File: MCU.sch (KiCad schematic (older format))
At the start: 66 parts, among them SW1 SW_Push, U1 STM32F407IGTx, Y1 12MHz, 20pF

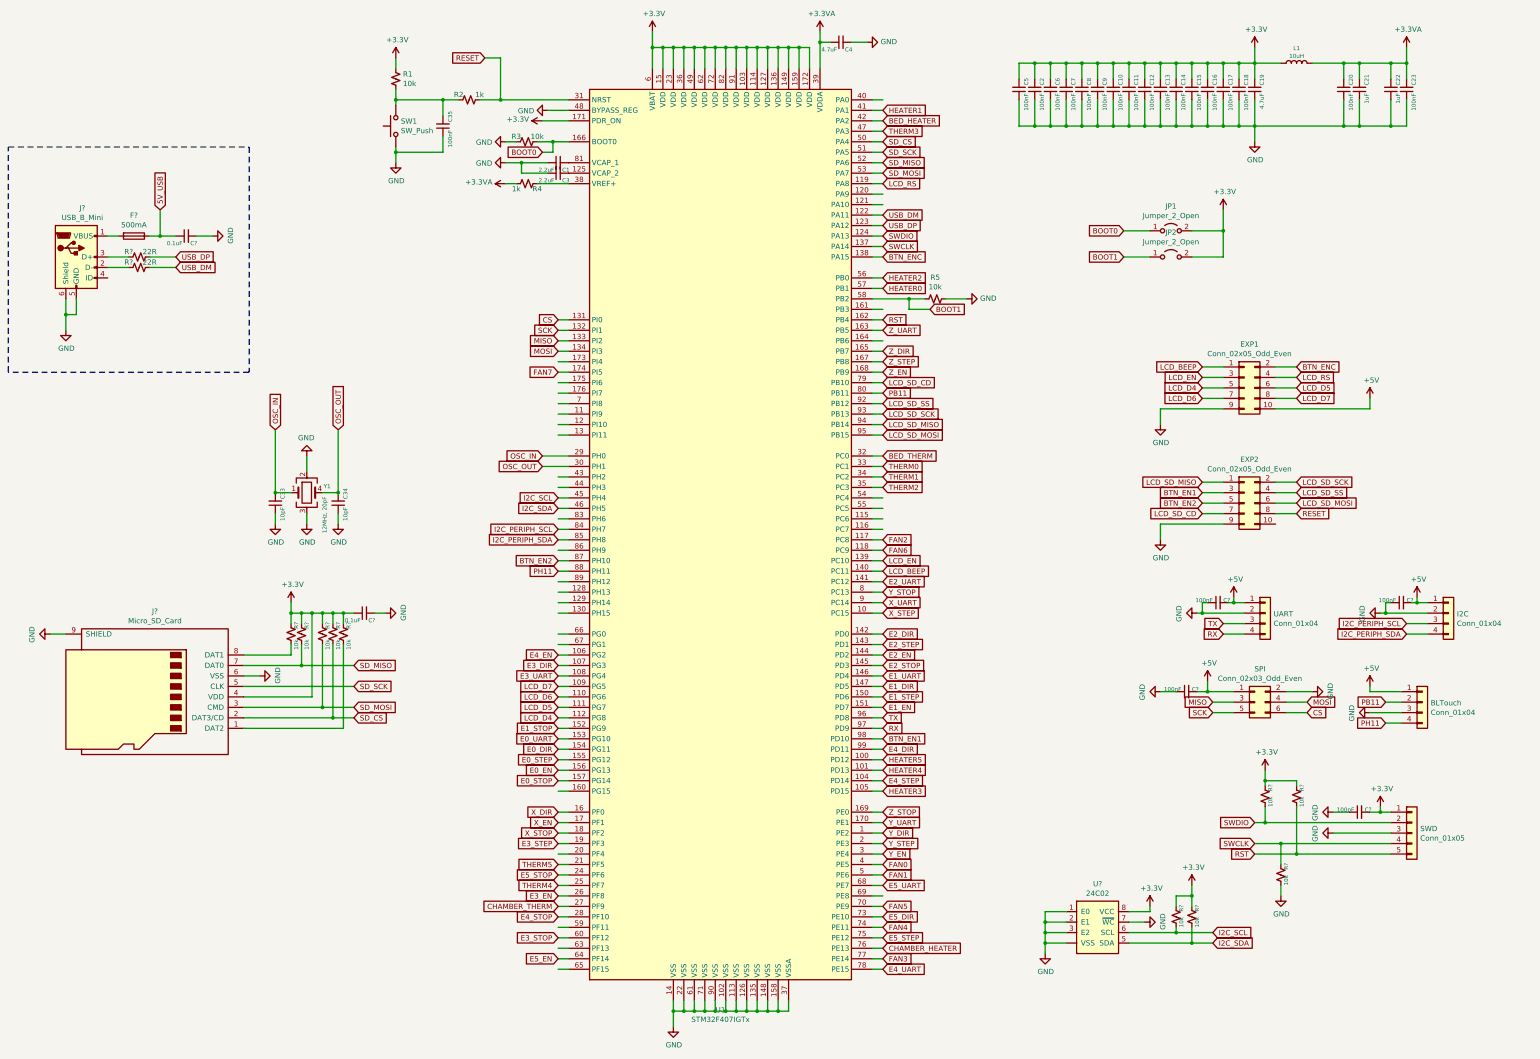
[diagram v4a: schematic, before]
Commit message: added raspberry pi header
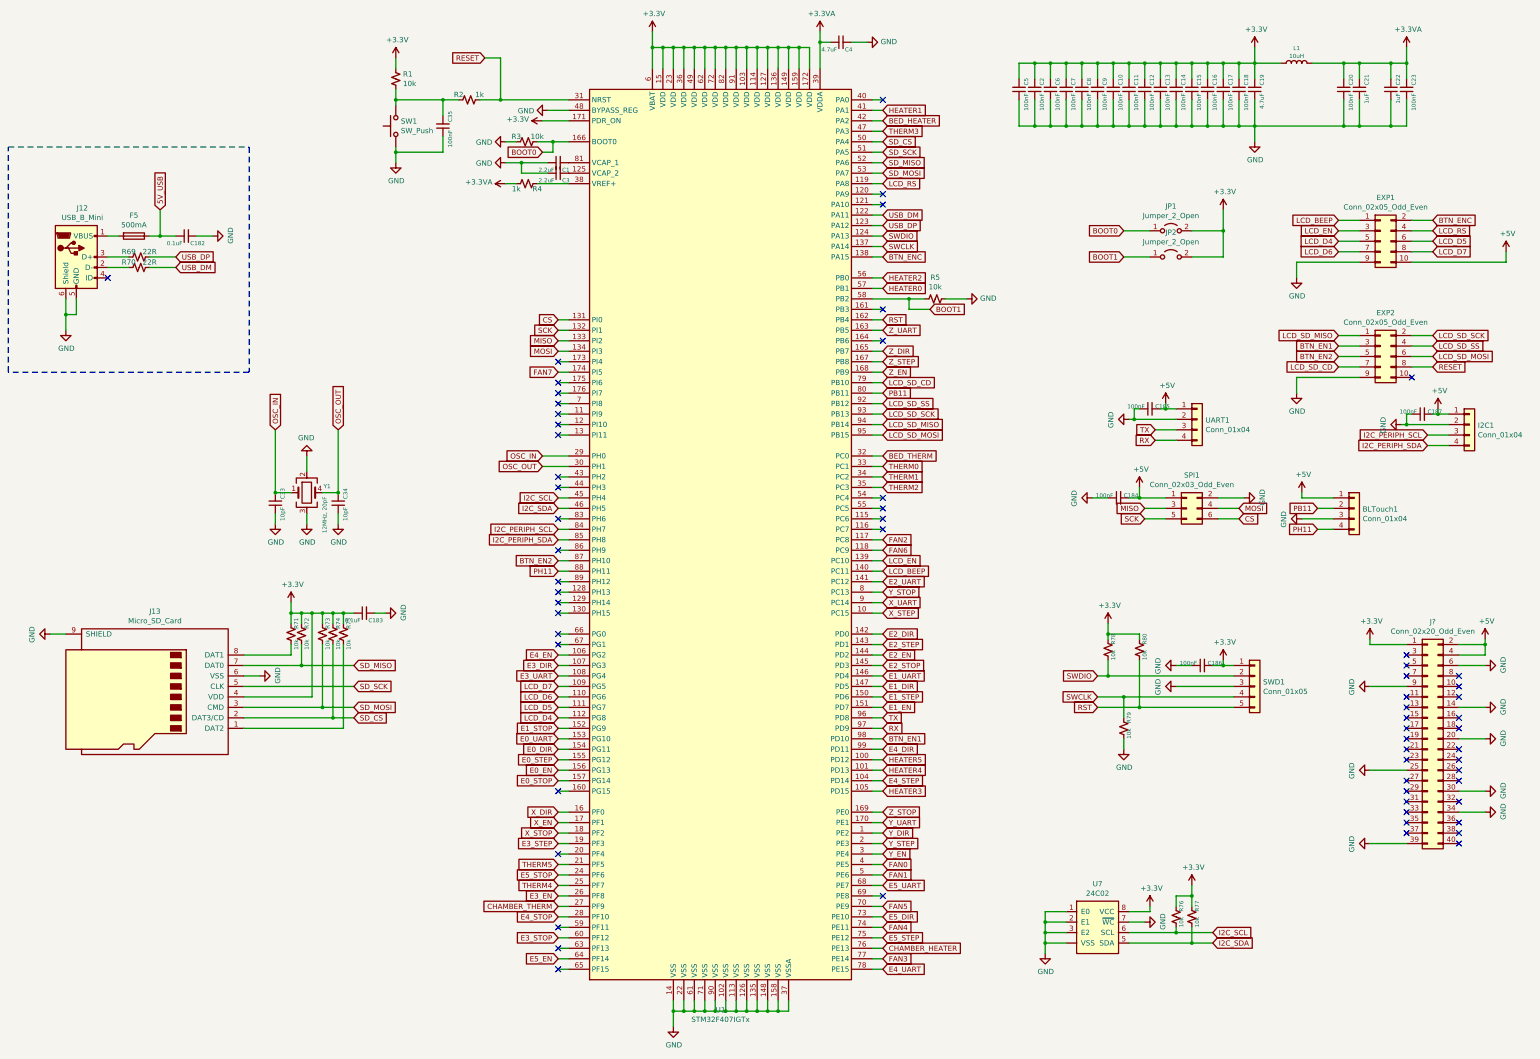
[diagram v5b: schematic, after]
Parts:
- added J?: Conn_02x20_Odd_Even, symbol Connector_Generic:Conn_02x20_Odd_Even
- gave numbers to parts that had none: 22
- renumbered BLTouch to BLTouch1, I2C to I2C1, SPI to SPI1, SWD to SWD1, UART to UART1
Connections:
- wire segments 465 -> 479
- no-connect marks 0 -> 63
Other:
- moved on the sheet: BLTouch1, C184, C185, C186, C187, EXP1, EXP2, I2C1, R78, R79, R80, SPI1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

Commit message: added library
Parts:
- gave numbers to parts that had none: 1
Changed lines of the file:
@@
 NoConn ~ 6350 5650
 $Comp
-L Connector_Generic:Conn_02x20_Odd_Even J?
+L Connector_Generic:Conn_02x20_Odd_Even J55
 U 1 1 61D58D2C
 P 14650 7450
-F 0 "J?" H 14700 8567 50  0000 C CNN
+F 0 "J55" H 14700 8567 50  0000 C CNN
 F 1 "Conn_02x20_Odd_Even" H 14700 8476 50  0000 C CNN
 F 2 "" H 14650 7450 50  0001 C CNN
@@
 $EndComp
 $Comp
-L power:+5V #PWR?
+L power:+5V #PWR0278
 U 1 1 61D5B6B4
 P 15200 6500
-F 0 "#PWR?" H 15200 6350 50  0001 C CNN
+F 0 "#PWR0278" H 15200 6350 50  0001 C CNN
 F 1 "+5V" H 15215 6673 50  0000 C CNN
 F 2 "" H 15200 6500 50  0001 C CNN
@@
 $EndComp
 $Comp
-L power:GND #PWR?
+L power:GND #PWR0279
 U 1 1 61D5BD7A
 P 15200 7950
-F 0 "#PWR?" H 15200 7700 50  0001 C CNN
+F 0 "#PWR0279" H 15200 7700 50  0001 C CNN
 F 1 "GND" H 15205 7777 50  0000 C CNN
 F 2 "" H 15200 7950 50  0001 C CNN
@@
 $EndComp
 $Comp
-L power:+3.3V #PWR?
+L power:+3.3V #PWR0280
 U 1 1 61D5BEF0
 P 14100 6500
-F 0 "#PWR?" H 14100 6350 50  0001 C CNN
+F 0 "#PWR0280" H 14100 6350 50  0001 C CNN
 F 1 "+3.3V" H 14115 6673 50  0000 C CNN
 F 2 "" H 14100 6500 50  0001 C CNN
@@
 Connection ~ 15200 6550
 $Comp
-L power:GND #PWR?
+L power:GND #PWR0281
 U 1 1 61E37426
 P 15200 6750
-F 0 "#PWR?" H 15200 6500 50  0001 C CNN
+F 0 "#PWR0281" H 15200 6500 50  0001 C CNN
 F 1 "GND" H 15205 6577 50  0000 C CNN
 F 2 "" H 15200 6750 50  0001 C CNN
@@
 $EndComp
 $Comp
-L power:GND #PWR?
+L power:GND #PWR0282
 U 1 1 61E375CC
 P 14100 6950
-F 0 "#PWR?" H 14100 6700 50  0001 C CNN
+F 0 "#PWR0282" H 14100 6700 50  0001 C CNN
 F 1 "GND" H 14105 6777 50  0000 C CNN
 F 2 "" H 14100 6950 50  0001 C CNN
@@
 $EndComp
 $Comp
-L power:GND #PWR?
+L power:GND #PWR0283
 U 1 1 61E378A8
 P 15200 7450
-F 0 "#PWR?" H 15200 7200 50  0001 C CNN
+F 0 "#PWR0283" H 15200 7200 50  0001 C CNN
 F 1 "GND" H 15205 7277 50  0000 C CNN
 F 2 "" H 15200 7450 50  0001 C CNN
@@
 $EndComp
 $Comp
-L power:GND #PWR?
+L power:GND #PWR0284
 U 1 1 61E37F4E
 P 15200 8150
-F 0 "#PWR?" H 15200 7900 50  0001 C CNN
+F 0 "#PWR0284" H 15200 7900 50  0001 C CNN
 F 1 "GND" H 15205 7977 50  0000 C CNN
 F 2 "" H 15200 8150 50  0001 C CNN
@@
 $EndComp
 $Comp
-L power:GND #PWR?
+L power:GND #PWR0285
 U 1 1 61E38209
 P 14100 7750
-F 0 "#PWR?" H 14100 7500 50  0001 C CNN
+F 0 "#PWR0285" H 14100 7500 50  0001 C CNN
 F 1 "GND" H 14105 7577 50  0000 C CNN
 F 2 "" H 14100 7750 50  0001 C CNN
@@
 $EndComp
 $Comp
-L power:GND #PWR?
+L power:GND #PWR0286
 U 1 1 61E38767
 P 14100 8450
-F 0 "#PWR?" H 14100 8200 50  0001 C CNN
+F 0 "#PWR0286" H 14100 8200 50  0001 C CNN
 F 1 "GND" H 14105 8277 50  0000 C CNN
 F 2 "" H 14100 8450 50  0001 C CNN
@@
 	15200 8150 14950 8150
 $Comp
-L power:GND #PWR?
+L power:GND #PWR0287
 U 1 1 62041588
 P 15200 7150
-F 0 "#PWR?" H 15200 6900 50  0001 C CNN
+F 0 "#PWR0287" H 15200 6900 50  0001 C CNN
 F 1 "GND" H 15205 6977 50  0000 C CNN
 F 2 "" H 15200 7150 50  0001 C CNN

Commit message: assigned some footprints
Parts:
- C10, C11, C12, C13, C14, C15, C16, C17, C18, C182, C183, C184, C185, C186, C187, C2, C20, C21, C22, C23, C35, C5, C6, C7, C8, C9: footprint (none) -> Capacitor_SMD:C_0603_1608Metric_Pad1.05x0.95mm_HandSolder
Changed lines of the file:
@@
 F 0 "C2" V 10808 1212 39  0000 R TNN
 F 1 "100nF" V 10808 1287 39  0000 L TNN
-F 2 "" H 10900 1250 50  0001 C CNN
+F 2 "Capacitor_SMD:C_0603_1608Metric_Pad1.05x0.95mm_HandSolder" H 10900 1250 50  0001 C CNN
 F 3 "~" H 10900 1250 50  0001 C CNN
 	1    10900 1250
@@
 F 0 "C6" V 10958 1212 39  0000 R TNN
 F 1 "100nF" V 10958 1287 39  0000 L TNN
-F 2 "" H 11050 1250 50  0001 C CNN
+F 2 "Capacitor_SMD:C_0603_1608Metric_Pad1.05x0.95mm_HandSolder" H 11050 1250 50  0001 C CNN
 F 3 "~" H 11050 1250 50  0001 C CNN
 	1    11050 1250
@@
 F 0 "C7" V 11108 1212 39  0000 R TNN
 F 1 "100nF" V 11108 1287 39  0000 L TNN
-F 2 "" H 11200 1250 50  0001 C CNN
+F 2 "Capacitor_SMD:C_0603_1608Metric_Pad1.05x0.95mm_HandSolder" H 11200 1250 50  0001 C CNN
 F 3 "~" H 11200 1250 50  0001 C CNN
 	1    11200 1250
@@
 F 0 "C8" V 11258 1212 39  0000 R TNN
 F 1 "100nF" V 11258 1287 39  0000 L TNN
-F 2 "" H 11350 1250 50  0001 C CNN
+F 2 "Capacitor_SMD:C_0603_1608Metric_Pad1.05x0.95mm_HandSolder" H 11350 1250 50  0001 C CNN
 F 3 "~" H 11350 1250 50  0001 C CNN
 	1    11350 1250
@@
 F 0 "C9" V 11408 1212 39  0000 R TNN
 F 1 "100nF" V 11408 1287 39  0000 L TNN
-F 2 "" H 11500 1250 50  0001 C CNN
+F 2 "Capacitor_SMD:C_0603_1608Metric_Pad1.05x0.95mm_HandSolder" H 11500 1250 50  0001 C CNN
 F 3 "~" H 11500 1250 50  0001 C CNN
 	1    11500 1250
@@
 F 0 "C10" V 11558 1212 39  0000 R TNN
 F 1 "100nF" V 11558 1287 39  0000 L TNN
-F 2 "" H 11650 1250 50  0001 C CNN
+F 2 "Capacitor_SMD:C_0603_1608Metric_Pad1.05x0.95mm_HandSolder" H 11650 1250 50  0001 C CNN
 F 3 "~" H 11650 1250 50  0001 C CNN
 	1    11650 1250
@@
 F 0 "C11" V 11708 1212 39  0000 R TNN
 F 1 "100nF" V 11708 1287 39  0000 L TNN
-F 2 "" H 11800 1250 50  0001 C CNN
+F 2 "Capacitor_SMD:C_0603_1608Metric_Pad1.05x0.95mm_HandSolder" H 11800 1250 50  0001 C CNN
 F 3 "~" H 11800 1250 50  0001 C CNN
 	1    11800 1250
@@
 F 0 "C12" V 11858 1212 39  0000 R TNN
 F 1 "100nF" V 11858 1287 39  0000 L TNN
-F 2 "" H 11950 1250 50  0001 C CNN
+F 2 "Capacitor_SMD:C_0603_1608Metric_Pad1.05x0.95mm_HandSolder" H 11950 1250 50  0001 C CNN
 F 3 "~" H 11950 1250 50  0001 C CNN
 	1    11950 1250
@@
 F 0 "C13" V 12008 1212 39  0000 R TNN
 F 1 "100nF" V 12008 1287 39  0000 L TNN
-F 2 "" H 12100 1250 50  0001 C CNN
+F 2 "Capacitor_SMD:C_0603_1608Metric_Pad1.05x0.95mm_HandSolder" H 12100 1250 50  0001 C CNN
 F 3 "~" H 12100 1250 50  0001 C CNN
 	1    12100 1250
@@
 F 0 "C14" V 12158 1212 39  0000 R TNN
 F 1 "100nF" V 12158 1287 39  0000 L TNN
-F 2 "" H 12250 1250 50  0001 C CNN
+F 2 "Capacitor_SMD:C_0603_1608Metric_Pad1.05x0.95mm_HandSolder" H 12250 1250 50  0001 C CNN
 F 3 "~" H 12250 1250 50  0001 C CNN
 	1    12250 1250
@@
 F 0 "C5" V 10658 1212 39  0000 R TNN
 F 1 "100nF" V 10658 1287 39  0000 L TNN
-F 2 "" H 10750 1250 50  0001 C CNN
+F 2 "Capacitor_SMD:C_0603_1608Metric_Pad1.05x0.95mm_HandSolder" H 10750 1250 50  0001 C CNN
 F 3 "~" H 10750 1250 50  0001 C CNN
 	1    10750 1250
@@
 F 0 "C15" V 12308 1212 39  0000 R TNN
 F 1 "100nF" V 12308 1287 39  0000 L TNN
-F 2 "" H 12400 1250 50  0001 C CNN
+F 2 "Capacitor_SMD:C_0603_1608Metric_Pad1.05x0.95mm_HandSolder" H 12400 1250 50  0001 C CNN
 F 3 "~" H 12400 1250 50  0001 C CNN
 	1    12400 1250
@@
 F 0 "C16" V 12458 1212 39  0000 R TNN
 F 1 "100nF" V 12458 1287 39  0000 L TNN
-F 2 "" H 12550 1250 50  0001 C CNN
+F 2 "Capacitor_SMD:C_0603_1608Metric_Pad1.05x0.95mm_HandSolder" H 12550 1250 50  0001 C CNN
 F 3 "~" H 12550 1250 50  0001 C CNN
 	1    12550 1250
@@
 F 0 "C17" V 12608 1212 39  0000 R TNN
 F 1 "100nF" V 12608 1287 39  0000 L TNN
-F 2 "" H 12700 1250 50  0001 C CNN
+F 2 "Capacitor_SMD:C_0603_1608Metric_Pad1.05x0.95mm_HandSolder" H 12700 1250 50  0001 C CNN
 F 3 "~" H 12700 1250 50  0001 C CNN
 	1    12700 1250
@@
 F 0 "C18" V 12758 1212 39  0000 R TNN
 F 1 "100nF" V 12758 1287 39  0000 L TNN
-F 2 "" H 12850 1250 50  0001 C CNN
+F 2 "Capacitor_SMD:C_0603_1608Metric_Pad1.05x0.95mm_HandSolder" H 12850 1250 50  0001 C CNN
 F 3 "~" H 12850 1250 50  0001 C CNN
 	1    12850 1250
@@
 F 0 "C20" V 13758 1212 39  0000 R TNN
 F 1 "100nF" V 13758 1287 39  0000 L TNN
-F 2 "" H 13850 1250 50  0001 C CNN
+F 2 "Capacitor_SMD:C_0603_1608Metric_Pad1.05x0.95mm_HandSolder" H 13850 1250 50  0001 C CNN
 F 3 "~" H 13850 1250 50  0001 C CNN
 	1    13850 1250
@@
 F 0 "C21" V 13908 1212 39  0000 R TNN
 F 1 "1uF" V 13908 1287 39  0000 L TNN
-F 2 "" H 14000 1250 50  0001 C CNN
+F 2 "Capacitor_SMD:C_0603_1608Metric_Pad1.05x0.95mm_HandSolder" H 14000 1250 50  0001 C CNN
 F 3 "~" H 14000 1250 50  0001 C CNN
 	1    14000 1250
@@
 F 0 "C22" V 14208 1212 39  0000 R TNN
 F 1 "1uF" V 14208 1287 39  0000 L TNN
-F 2 "" H 14300 1250 50  0001 C CNN
+F 2 "Capacitor_SMD:C_0603_1608Metric_Pad1.05x0.95mm_HandSolder" H 14300 1250 50  0001 C CNN
 F 3 "~" H 14300 1250 50  0001 C CNN
 	1    14300 1250
@@
 F 0 "C23" V 14358 1212 39  0000 R TNN
 F 1 "100nF" V 14358 1287 39  0000 L TNN
-F 2 "" H 14450 1250 50  0001 C CNN
+F 2 "Capacitor_SMD:C_0603_1608Metric_Pad1.05x0.95mm_HandSolder" H 14450 1250 50  0001 C CNN
 F 3 "~" H 14450 1250 50  0001 C CNN
 	1    14450 1250
@@
 F 0 "C35" V 5158 1562 39  0000 R TNN
 F 1 "100nF" V 5158 1637 39  0000 L TNN
-F 2 "" H 5250 1600 50  0001 C CNN
+F 2 "Capacitor_SMD:C_0603_1608Metric_Pad1.05x0.95mm_HandSolder" H 5250 1600 50  0001 C CNN
 F 3 "~" H 5250 1600 50  0001 C CNN
 	1    5250 1600
@@
 F 0 "C182" V 2708 2612 39  0000 R TNN
 F 1 "0.1uF" V 2708 2687 39  0000 L TNN
-F 2 "" H 2800 2650 50  0001 C CNN
+F 2 "Capacitor_SMD:C_0603_1608Metric_Pad1.05x0.95mm_HandSolder" H 2800 2650 50  0001 C CNN
 F 3 "~" H 2800 2650 50  0001 C CNN
 	1    2800 2650
@@
 F 0 "C183" V 4408 6212 39  0000 R TNN
 F 1 "0.1uF" V 4408 6287 39  0000 L TNN
-F 2 "" H 4500 6250 50  0001 C CNN
+F 2 "Capacitor_SMD:C_0603_1608Metric_Pad1.05x0.95mm_HandSolder" H 4500 6250 50  0001 C CNN
 F 3 "~" H 4500 6250 50  0001 C CNN
 	1    4500 6250
@@
 F 0 "C187" V 14600 4300 39  0000 R TNN
 F 1 "100nF" V 14600 4400 39  0000 L TNN
-F 2 "" H 14600 4350 50  0001 C CNN
+F 2 "Capacitor_SMD:C_0603_1608Metric_Pad1.05x0.95mm_HandSolder" H 14600 4350 50  0001 C CNN
 F 3 "~" H 14600 4350 50  0001 C CNN
 	1    14600 4350
@@
 F 0 "C184" V 11700 5100 39  0000 R TNN
 F 1 "100nF" V 11700 5200 39  0000 L TNN
-F 2 "" H 11700 5150 50  0001 C CNN
+F 2 "Capacitor_SMD:C_0603_1608Metric_Pad1.05x0.95mm_HandSolder" H 11700 5150 50  0001 C CNN
 F 3 "~" H 11700 5150 50  0001 C CNN
 	1    11700 5150
@@
 F 0 "C185" V 12000 4250 39  0000 R TNN
 F 1 "100nF" V 12000 4350 39  0000 L TNN
-F 2 "" H 12000 4300 50  0001 C CNN
+F 2 "Capacitor_SMD:C_0603_1608Metric_Pad1.05x0.95mm_HandSolder" H 12000 4300 50  0001 C CNN
 F 3 "~" H 12000 4300 50  0001 C CNN
 	1    12000 4300
@@
 F 0 "C186" V 12500 6700 39  0000 R TNN
 F 1 "100nF" V 12500 6800 39  0000 L TNN
-F 2 "" H 12500 6750 50  0001 C CNN
+F 2 "Capacitor_SMD:C_0603_1608Metric_Pad1.05x0.95mm_HandSolder" H 12500 6750 50  0001 C CNN
 F 3 "~" H 12500 6750 50  0001 C CNN
 	1    12500 6750
